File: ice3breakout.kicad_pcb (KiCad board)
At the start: 2 copper layers, 50 x 50 mm, 16 parts, among them CON1 AVR-ISP-6, CON2 AVR-JTAG-10, CON3 AVR-PDI-6, CON4 USB-MICRO-B, P1 Jtag ICE3, P2 Cortex M0 debug, P3 ice3 expansion, P4 CONN_02X03, SW1 SW_PUSH, U1 AP1117D33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

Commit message: Added schematic as pdf, and manufacturing files
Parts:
- removed REF**: Symbol_OSHW-Logo_CopperTop_BIG, Symbols:Symbol_OSHW-Logo_CopperTop_BIG
- added P5: Supply, Pin_Headers:Pin_Header_Straight_1x02, F.Cu at (151.6, 118.1)
- added P6: GND, Pin_Headers:Pin_Header_Straight_1x01, F.Cu at (140.1, 82.2)
- P4: value CONN_02X03 -> Supply select
- U1, U2: footprint Housings_SOT-89:SOT89-3_Housing_Handsoldering -> SMD_Packages:SOT-223
- moved C1 36.0 mm to (148.9, 119.7), turned to 270 degrees
- moved P2 35.9 mm to (111.6, 103.0)
- moved P4 35.5 mm to (144.7, 108.9), turned to 90 degrees
- moved U1 34.9 mm to (144.4, 117.0)
- moved CON4 33.6 mm to (145.7, 128.4)
- moved C2 26.0 mm to (139.9, 119.8), turned to 270 degrees
- moved C3 17.8 mm to (139.9, 111.3), turned to 180 degrees
- moved U2 16.1 mm to (135.4, 117.0)
- moved CON2 4.55 mm to (128.7, 102.8)
- moved SW1 1.53 mm to (146.4, 100.4)
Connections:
- CON2 pad 6: Net-(CON2-Pad6) -> /RST
- CON3 pad 1: Net-(CON3-Pad1) -> Net-(CON1-Pad1)
- CON3 pad 5: Net-(CON3-Pad5) -> /RST
- P1 pad 10: Net-(P1-Pad10) -> GND
- P3 pad 10: Net-(P1-Pad10) -> GND
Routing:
- net Net-(CON1-Pad1): track 40.8 -> 91.5 mm, vias 1 -> 3
- net /RST: track 65.8 -> 115.6 mm, vias 2 -> 4
- net Net-(P1-Pad10): track 39.6 -> 0.00 mm, vias 2 -> 0
- net VCC: track 62.2 -> 91.1 mm, vias 3 -> 0
- net +5V: track 0.00 -> 23.7 mm
- net +3V3: track 0.00 -> 22.6 mm
- net +1V8: track 0.00 -> 16.7 mm
- net Net-(R1-Pad1): track 2.92 -> 10.3 mm
- net GND: track 0.00 -> 6.67 mm
- net Net-(CON1-Pad3): track 70.2 -> 65.8 mm, vias 2 -> 3
- net Net-(CON2-Pad7): track 39.0 -> 42.1 mm, vias 1 -> 2
- net Net-(CON2-Pad5): track 61.0 -> 63.3 mm
- net Net-(CON1-Pad4): track 63.6 -> 65.0 mm
- net Net-(CON2-Pad8): track 40.8 -> 39.8 mm, vias 1 -> 2
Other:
- board text added: "+5V in"
- board text added: "Scope GND"
- board text added: "Supply only"

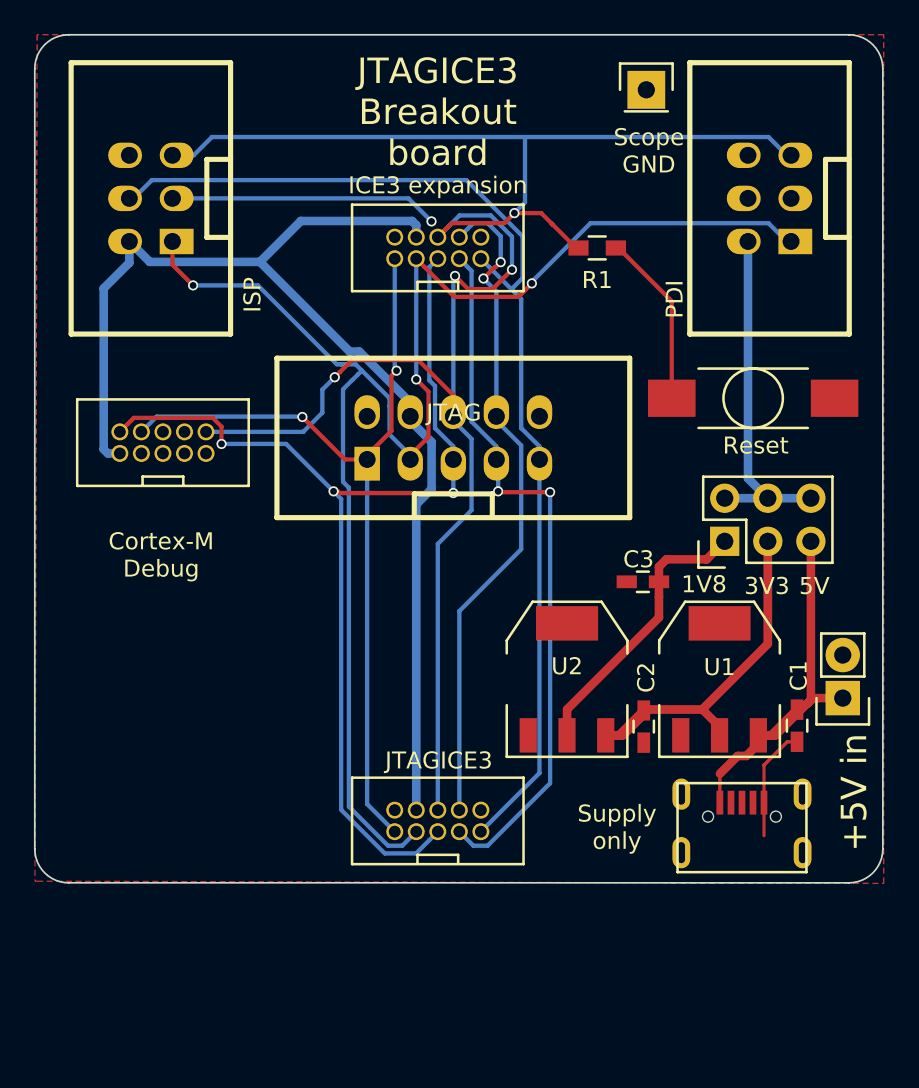
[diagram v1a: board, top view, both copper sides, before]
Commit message: Added pin legend to silkscreen, OSHW logo to bottom layer copper
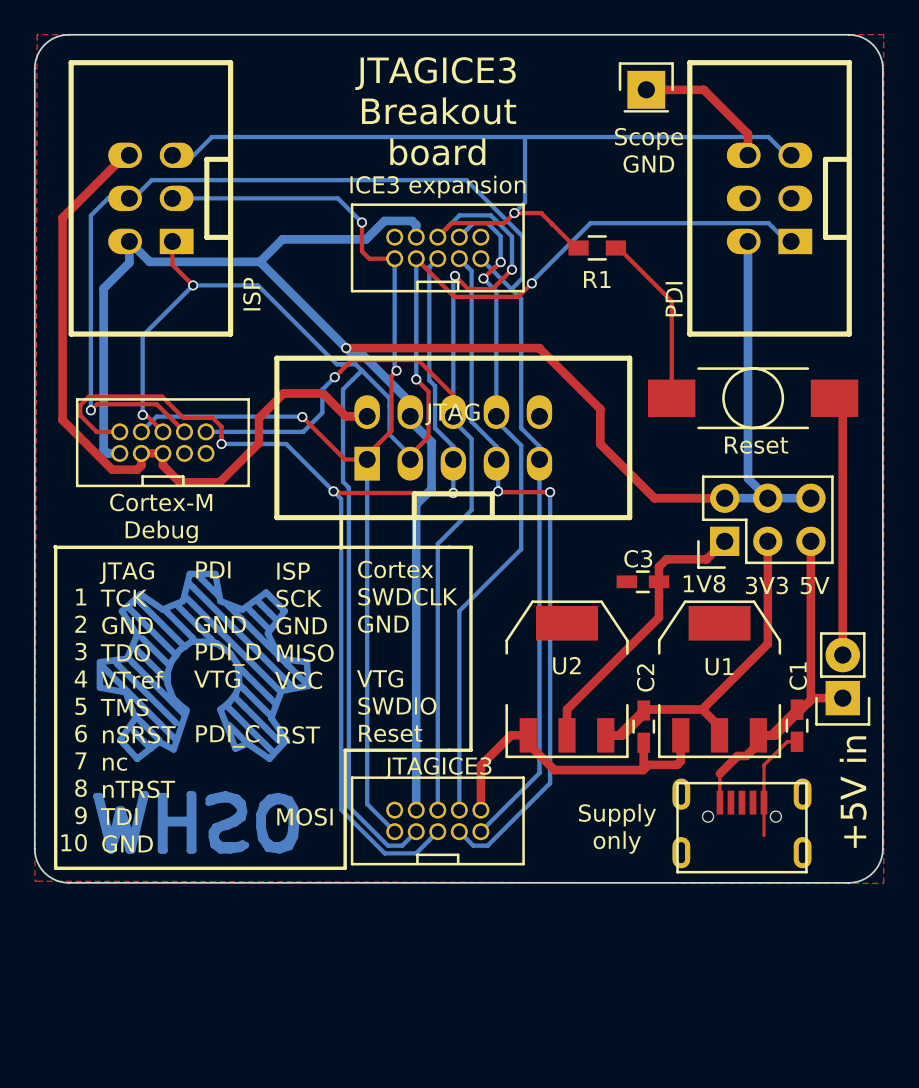
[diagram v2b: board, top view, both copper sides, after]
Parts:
- added REF**: Symbol_OSHW-Logo_CopperTop_BIG, Symbols:Symbol_OSHW-Logo_CopperTop_BIG, B.Cu at (113.8, 97.6)
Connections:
- P2 pad 6: Net-(P2-Pad6) -> Net-(CON1-Pad1)
- P2 pad 8: Net-(P2-Pad8) -> Net-(CON1-Pad4)
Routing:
- net GND: track 6.67 -> 92.0 mm
- net VCC: track 91.1 -> 118.3 mm, vias 0 -> 1
- net Net-(CON1-Pad4): track 65.0 -> 85.6 mm, vias 0 -> 1
- net Net-(CON1-Pad1): track 91.5 -> 102.0 mm, vias 3 -> 4
- net Net-(CON2-Pad5): track 63.3 -> 69.4 mm
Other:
- board text added: "1 2 3 4 5 6 7 8 9 10"
- board text added: "Cortex SWDCLK GND VTG SWDIO Reset"
- board text added: "ISP SCK GND MISO VCC RST MOSI"
- board text added: "JTAG TCK GND TDO VTref TMS nSRST nc nTRST TDI GND"
- board text added: "PDI GND PDI_D VTG PDI_C"

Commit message: closes #1, closes #2, closes #3
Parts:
- removed CON3: AVR-PDI-6, w_conn_strip:vasch_strip_3x2
- added C4: C, Capacitors_SMD:C_0603_HandSoldering, F.Cu at (139.9, 111.7)
- added REF**: MountingHole_3-5mm, Mounting_Holes:MountingHole_3-5mm, F.Cu at (150.2, 82.8)
- added REF**: MountingHole_3-5mm, Mounting_Holes:MountingHole_3-5mm, F.Cu at (107.7, 82.7)
- added REF**: MountingHole_3-5mm, Mounting_Holes:MountingHole_3-5mm, F.Cu at (107.7, 125.3)
- added REF**: MountingHole_3-5mm, Mounting_Holes:MountingHole_3-5mm, F.Cu at (150.3, 125.2)
- moved P2 36.0 mm to (146.4, 94.1), turned to 90 degrees
- moved P6 27.4 mm to (135.6, 109.2)
- moved SW1 16.7 mm to (139.7, 85.1)
- moved C2 10.5 mm to (148.8, 114.2)
- moved P3 9.92 mm to (137.4, 94.1), turned to 90 degrees
- moved CON2 8.85 mm to (127.1, 94.1), turned to 90 degrees
- moved C3 8.10 mm to (139.8, 119.4), turned to 90 degrees
- moved REF** 7.95 mm to (114.5, 89.7)
- moved CON1 6.14 mm to (113.7, 94.1)
- moved CON4 4.08 mm to (141.6, 128.5)
- moved R1 3.66 mm to (136.9, 87.9), turned to 0 degrees
- moved P4 2.95 mm to (143.0, 106.4)
- moved P5 1.39 mm to (151.5, 116.7), turned to 0 degrees
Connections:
- C3 pad 1: +1V8 -> +5V
- U2 pad 3: +3V3 -> +5V
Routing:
- net GND: track 92.0 -> 32.5 mm
- net /RST: track 115.6 -> 73.3 mm
- net Net-(CON1-Pad1): track 102.0 -> 75.1 mm, vias 4 -> 1
- net +5V: track 23.7 -> 39.1 mm, vias 0 -> 1
- net Net-(CON2-Pad7): track 42.1 -> 57.3 mm
- net Net-(CON2-Pad8): track 39.8 -> 48.7 mm, vias 2 -> 1
- net VCC: track 118.3 -> 127.1 mm, vias 1 -> 0
- net Net-(R1-Pad1): track 10.3 -> 3.23 mm
- net Net-(CON2-Pad5): track 69.4 -> 63.0 mm
- net +3V3: track 22.6 -> 17.8 mm
- net Net-(CON1-Pad4): track 85.6 -> 82.0 mm, vias 1 -> 2
- net Net-(CON1-Pad3): track 65.5 -> 63.5 mm, vias 3 -> 1
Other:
- net class Default: clearance 0.2 -> 0.1905
- net class Power: clearance 0.2 -> 0.1905
- rule trace_clearance: 0.2 -> 0.1905
- board text added: "1"
- board text added: "Cortex VCC SWDIO GND SWDCLK GND SWO (key) NC - Reset"
- board text added: "Cortex-M"
- board text added: "ISP MISO VCC SCK MOSI RST GND"
- board text added: "ISP/PDI"
- board text added: "JTAG / ICE3"
- board text added: "PDI PDI_D VCC nc nc PDI_C GND"
- board text removed: "Cortex SWDCLK GND VTG SWDIO Reset"
- board text removed: "Cortex-M Debug"
- board text removed: "ICE3 expansion"
- board text removed: "ISP"
- board text removed: "ISP SCK GND MISO VCC RST MOSI"
- board text removed: "PDI"
- board text removed: "PDI GND PDI_D VTG PDI_C"

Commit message: Added extra GND pins
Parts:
- added P7: GND, Pin_Headers:Pin_Header_Straight_1x01, F.Cu at (151.8, 88.3)
- added P8: GND, Pin_Headers:Pin_Header_Straight_1x01, F.Cu at (106.2, 88.3)
- C1, C2, C3, C4: value C -> 100nF
- moved SW1 1.45 mm to (139.6, 83.7)
- moved R1 1.28 mm to (137.2, 86.7)
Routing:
- net GND: track 32.5 -> 13.0 mm
- net /RST: track 73.3 -> 74.9 mm
- net Net-(R1-Pad1): track 3.23 -> 4.14 mm
